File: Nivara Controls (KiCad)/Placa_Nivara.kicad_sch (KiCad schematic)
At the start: 3 parts, among them U2 ESP32-S3-WROOM-1

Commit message: actual
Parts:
- added R25, R26, R27: R_0603, PCM_Resistor_SMD_AKL:R_0603_1608Metric, symbol PCM_Resistor_US_AKL:R_0603
- C4: Capacidad (none) -> 1uF
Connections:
- net +3.3V: now also R25.1, R26.1, R27.1
- net 0mA__10mA_module/SCLK: now also U2.17 (GPIO9/TOUCH9/ADC1_CH8/FSPIHD/SUBSPIHD), R25.2; no longer U2.12 (GPIO8/TOUCH8/ADC1_CH7/SUBSPICS1)
- net 0mA__10mA_module/SDA: now also U2.12 (GPIO8/TOUCH8/ADC1_CH7/SUBSPICS1), R26.2; no longer U2.17 (GPIO9/TOUCH9/ADC1_CH8/FSPIHD/SUBSPIHD)
- net RUN/STOP: now also U2.30 (SPIDQS/GPIO37/FSPIQ/SUBSPIQ), R27.2
- net OUT__4__20/ASLK_4-20: no longer names the net of U2.7 (GPIO7/TOUCH7/ADC1_CH6)
- net OUT__4__20/SDA_4-20: no longer names the net of U2.6 (GPIO6/TOUCH6/ADC1_CH5)
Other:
- moved on the sheet: C4

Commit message: Actualización
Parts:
- removed R25, R26, R27: R_0603, PCM_Resistor_SMD_AKL:R_0603_1608Metric, symbol PCM_Resistor_US_AKL:R_0603
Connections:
- net 0v__10v_Module/D_0v__10v: now also U2.4 (GPIO4/TOUCH4/ADC1_CH3); no longer U2.38 (GPIO2/TOUCH2/ADC1_CH1)
- net 0v__32v__module/D_0v__32v__: now also U2.15 (GPIO3/TOUCH3/ADC1_CH2); no longer U2.39 (GPIO1/TOUCH1/ADC1_CH0)
- net 4mA__20mA_module/A_4mA_20mA_Out: now also U2.5 (GPIO5/TOUCH5/ADC1_CH4); no longer U2.15 (GPIO3/TOUCH3/ADC1_CH2)
- net Digit_module/Digit_input1_--: now also U2.6 (GPIO6/TOUCH6/ADC1_CH5); no longer U2.4 (GPIO4/TOUCH4/ADC1_CH3)
- net Digit_module/Digit_input_2--: now also U2.7 (GPIO7/TOUCH7/ADC1_CH6); no longer U2.5 (GPIO5/TOUCH5/ADC1_CH4)
- net Driver_RS485/UART_IN: now also U2.10 (GPIO17/U1TXD/ADC2_CH6); no longer U2.37 (U0TXD/GPIO43/CLK_OUT1)
- net Driver_RS485/UART_OUT: now also U2.11 (GPIO18/U1RXD/ADC2_CH7/CLK_OUT3); no longer U2.36 (U0RXD/GPIO44/CLK_OUT2)
- net RUN/STOP: no longer U2.30 (SPIDQS/GPIO37/FSPIQ/SUBSPIQ)
- net Output_PNP/PNP_input_0: now reaches U2.23 (GPIO21)
- net Output_PNP/PNP_input_1: now reaches U2.31 (GPIO38/FSPIWP/SUBSPIWP)
- new net Output_NPN/NPN_Input_1: U2.38 (GPIO2/TOUCH2/ADC1_CH1)
- new net Output_NPN/NPN_input_0: U2.39 (GPIO1/TOUCH1/ADC1_CH0)
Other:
- sheet Output_NPN ports: added NPN_Input_1, NPN_input_0, NPN_output_0, NPN_output_1; removed none
- sheet Output_PNP ports: added PNP_Output_0, PNP_Output_1, PNP_input_0, PNP_input_1; removed none
- moved on the sheet: C4, R1, U2

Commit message: Actual
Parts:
- added R25: R_0603, PCM_Resistor_SMD_AKL:R_0603_1608Metric, symbol PCM_Resistor_US_AKL:R_0603
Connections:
- net +3.3V: now also R25.1
- net RUN/STOP: now also U2.28 (SPIIO6/GPIO35/FSPID/SUBSPID), R25.2
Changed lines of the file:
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@@
 		(color 0 0 0 0)
 	)
+	(junction
+		(at 67.31 107.95)
+		(diameter 0)
+		(color 0 0 0 0)
+	)
 	(wire
 		(pts
@@
 	(wire
 		(pts
+			(xy 67.31 109.22) (xy 78.74 109.22)
+		)
+		(stroke
+			(width 0)
+			(type default)
+		)
+	)
+	(wire
+		(pts
 			(xy 193.04 88.9) (xy 170.18 88.9)
 		)
@@
 	(wire
 		(pts
+			(xy 63.5 107.95) (xy 67.31 107.95)
+		)
+		(stroke
+			(width 0)
+			(type default)
+		)
+	)
+	(wire
+		(pts
 			(xy 129.54 134.62) (xy 132.08 134.62)
 		)
@@
 	(wire
 		(pts
+			(xy 67.31 96.52) (xy 67.31 99.06)
+		)
+		(stroke
+			(width 0)
+			(type default)
+		)
+	)
+	(wire
+		(pts
 			(xy 203.2 68.58) (xy 203.2 52.07)
 		)
@@
 	(wire
 		(pts
+			(xy 67.31 107.95) (xy 67.31 109.22)
+		)
+		(stroke
+			(width 0)
+			(type default)
+		)
+	)
+	(wire
+		(pts
 			(xy 180.34 109.22) (xy 180.34 119.38)
 		)
@@
 		(pts
 			(xy 209.55 127) (xy 191.77 127)
+		)
+		(stroke
+			(width 0)
+			(type default)
+		)
+	)
+	(wire
+		(pts
+			(xy 67.31 106.68) (xy 67.31 107.95)
 		)
 		(stroke
@@
 	(hierarchical_label "RUN{slash}STOP"
 		(shape bidirectional)
-		(at 74.93 60.96 180)
+		(at 63.5 107.95 180)
 		(effects
 			(font
@@
 	)
 	(symbol
+		(lib_id "PCM_Resistor_US_AKL:R_0603")
+		(at 67.31 102.87 0)
+		(unit 1)
+		(exclude_from_sim no)
+		(in_bom yes)
+		(on_board yes)
+		(dnp no)
+		(property "Reference" "R25"
+			(at 69.85 101.5999 0)
+			(effects
+				(font
+					(size 1.27 1.27)
+				)
+				(justify left)
+			)
+		)
+		(property "Value" "R_0603"
+			(at 69.85 103.378 0)
+			(effects
+				(font
+					(size 1.27 1.27)
+				)
+				(justify left)
+			)
+		)
+		(property "Footprint" "PCM_Resistor_SMD_AKL:R_0603_1608Metric"
+			(at 67.31 114.3 0)
+			(effects
+				(font
+					(size 1.27 1.27)
+				)
+				(hide yes)
+			)
+		)
+		(property "Datasheet" "~"
+			(at 67.31 102.87 0)
+			(effects
+				(font
+					(size 1.27 1.27)
+				)
+				(hide yes)
+			)
+		)
+		(property "Description" "SMD 0603 Chip Resistor, US Symbol, Alternate KiCad Library"
+			(at 67.31 102.87 0)
+			(effects
+				(font
+					(size 1.27 1.27)
+				)
+				(hide yes)
+			)
+		)
+		(property "Part Number" ""
+			(at 67.31 102.87 0)
+			(effects
+				(font
+					(size 1.27 1.27)
+				)
+				(hide yes)
+			)
+		)
+		(property "Capacidad" "10k"
+			(at 71.628 105.156 0)
+			(effects
+				(font
+					(size 1.27 1.27)
+				)
+			)
+		)
+		(pin "1"
+		)
+		(pin "2"
+		)
+		(instances
+			(project "Nivara Controls"
+				(path "/42622735-4343-4315-af64-a45701a752b6/711b914f-41ac-411e-bef3-8ade05c9a19b"
+					(reference "R25")
+					(unit 1)
+				)
+			)
+		)
+	)
+	(symbol
 		(lib_id "power:GND")
 		(at 102.87 121.92 0)
@@
 					(unit 1)
 				)
+			)
+		)
+	)
+	(symbol
+		(lib_id "power:+3.3V")
+		(at 67.31 96.52 0)
+		(unit 1)
+		(exclude_from_sim no)
+		(in_bom yes)
+		(on_board yes)
+		(dnp no)
+		(fields_autoplaced yes)
+		(property "Reference" "#PWR062"
+			(at 67.31 100.33 0)
+			(effects
+				(font
+					(size 1.27 1.27)
+				)
+				(hide yes)
+			)
+		)
+		(property "Value" "+3.3V"
+			(at 67.31 91.44 0)
+			(effects
+				(font
+					(size 1.27 1.27)
+				)
+			)
+		)
+		(property "Footprint" ""
+			(at 67.31 96.52 0)
+			(effects
+				(font
+					(size 1.27 1.27)
+				)
+				(hide yes)
+			)
+		)
+		(property "Datasheet" ""
+			(at 67.31 96.52 0)
+			(effects
+				(font
+					(size 1.27 1.27)
+				)
+				(hide yes)
+			)
+		)
+		(property "Description" "Power symbol creates a global label with name \"+3.3V\""
+			(at 67.31 96.52 0)
+			(effects
+				(font
+					(size 1.27 1.27)
+				)
+				(hide yes)
+			)
+		)
+		(pin "1"
+		)
+		(instances
+			(project "Nivara Controls"
+				(path "/42622735-4343-4315-af64-a45701a752b6/711b914f-41ac-411e-bef3-8ade05c9a19b"
+					(reference "#PWR062")
+					(unit 1)
+				)

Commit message: Trabajando en PCB
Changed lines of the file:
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@@
 	(wire
 		(pts
-			(xy 102.87 120.65) (xy 102.87 121.92)
+			(xy 111.76 120.65) (xy 111.76 121.92)
 		)
 		(stroke
@@
 	(wire
 		(pts
-			(xy 130.81 128.27) (xy 130.81 119.38)
+			(xy 129.54 128.27) (xy 129.54 119.38)
 		)
 		(stroke
@@
 	(wire
 		(pts
-			(xy 102.87 120.65) (xy 124.46 120.65)
+			(xy 111.76 120.65) (xy 124.46 120.65)
 		)
 		(stroke
@@
 	(wire
 		(pts
-			(xy 180.34 119.38) (xy 130.81 119.38)
+			(xy 180.34 119.38) (xy 129.54 119.38)
 		)
 		(stroke
@@
 	(wire
 		(pts
-			(xy 132.08 128.27) (xy 130.81 128.27)
+			(xy 132.08 128.27) (xy 129.54 128.27)
 		)
 		(stroke
@@
 	(symbol
 		(lib_id "power:GND")
-		(at 102.87 121.92 0)
+		(at 111.76 121.92 0)
 		(unit 1)
 		(exclude_from_sim no)
@@
 		(dnp no)
 		(property "Reference" "#PWR010"
-			(at 102.87 128.27 0)
+			(at 111.76 128.27 0)
 			(effects
 				(font
@@
 		)
 		(property "Value" "GND"
-			(at 102.87 127 0)
+			(at 111.76 127 0)
 			(effects
 				(font
@@
 		)
 		(property "Footprint" ""
-			(at 102.87 121.92 0)
+			(at 111.76 121.92 0)
 			(effects
 				(font
@@
 		)
 		(property "Datasheet" ""
-			(at 102.87 121.92 0)
+			(at 111.76 121.92 0)
 			(effects
 				(font
@@
 		)
 		(property "Description" "Power symbol creates a global label with name \"GND\" , ground"
-			(at 102.87 121.92 0)
-			(effects
-				(font
+			(at 111.76 121.92 0)
+			(effects
+				(font

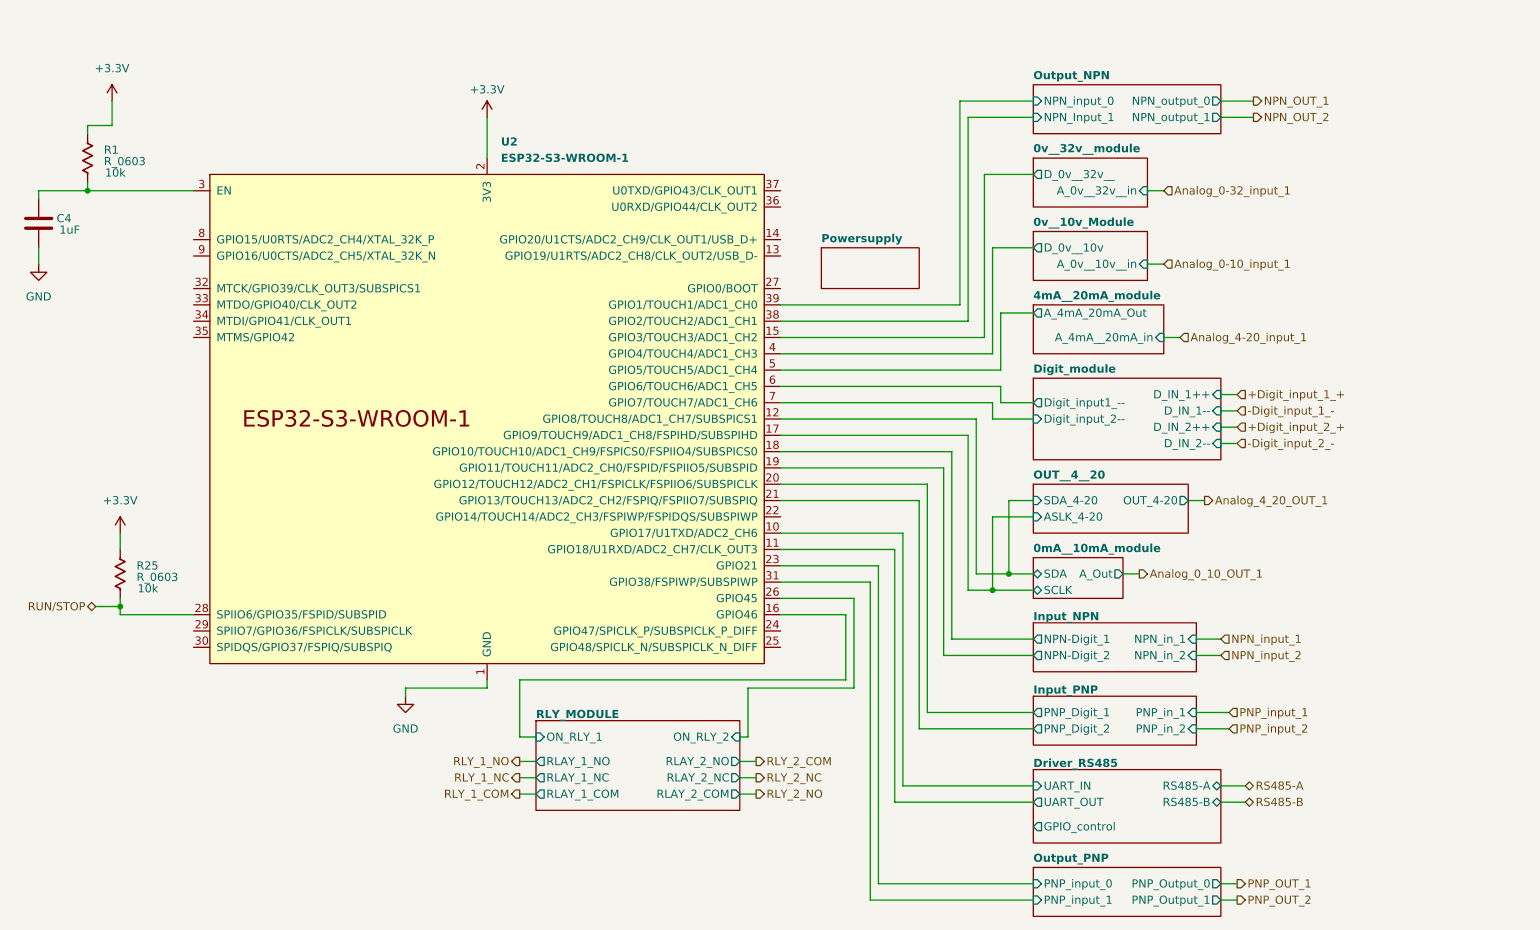
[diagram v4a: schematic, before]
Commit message: Actualizació Orden de componentes
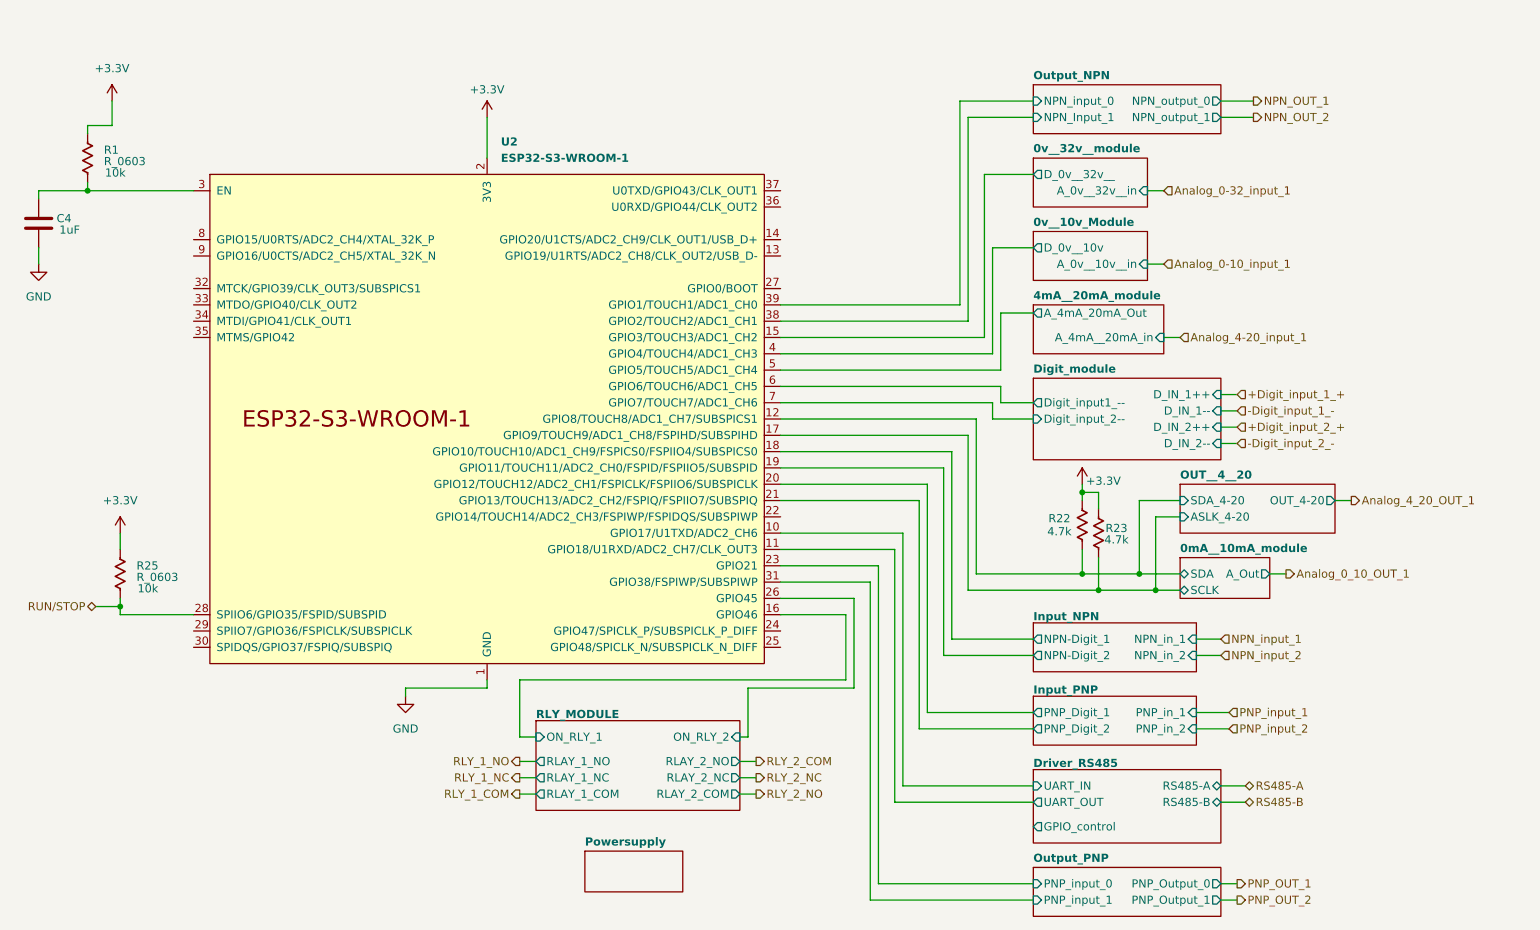
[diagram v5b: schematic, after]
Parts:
- added R22, R23: R_0603, PCM_Resistor_SMD_AKL:R_0603_1608Metric, symbol PCM_Resistor_US_AKL:R_0603
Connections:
- net +3.3V: now also R22.2, R23.2
- net 0mA__10mA_module/SCLK: now also R23.1
- net 0mA__10mA_module/SDA: now also R22.1

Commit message: rutas
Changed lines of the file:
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@@
 	(wire
 		(pts
-			(xy 256.54 91.44) (xy 259.08 91.44)
+			(xy 256.54 91.44) (xy 261.62 91.44)
 		)
 		(stroke
@@
 	(wire
 		(pts
-			(xy 246.38 102.87) (xy 248.92 102.87)
+			(xy 246.38 102.87) (xy 251.46 102.87)
 		)
 		(stroke
@@
 	(hierarchical_label "Analog_4_20_OUT_1"
 		(shape output)
-		(at 259.08 91.44 0)
+		(at 261.62 91.44 0)
 		(effects
 			(font
@@
 	(hierarchical_label "Analog_0_10_OUT_1"
 		(shape output)
-		(at 248.92 102.87 0)
-		(effects
-			(font
+		(at 251.46 102.87 0)
+		(effects
+			(font
